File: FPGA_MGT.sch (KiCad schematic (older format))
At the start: 51 parts, among them J2 HIROSE_U.FL-R-SMT-1(10), J5 HIROSE_U.FL-R-SMT-1(10), U1 XC7A100T-2FGG484C

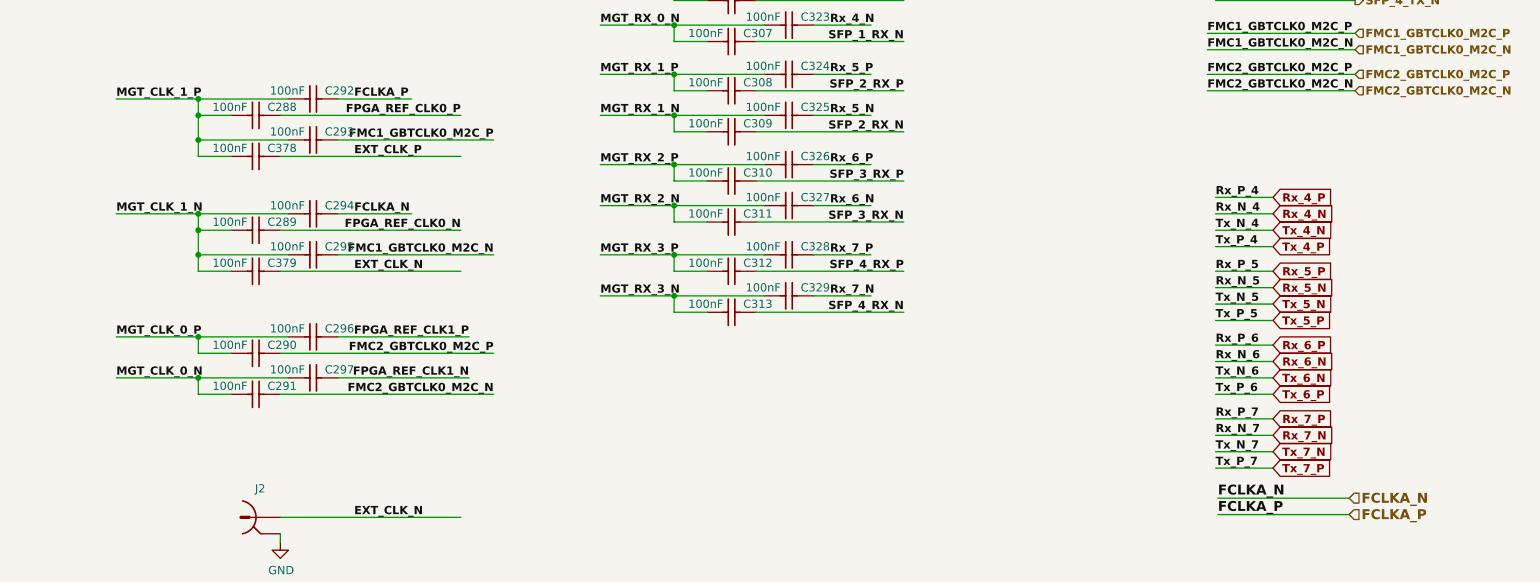
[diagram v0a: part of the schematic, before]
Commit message: added SI570, U39 3V3 -> 3V3P
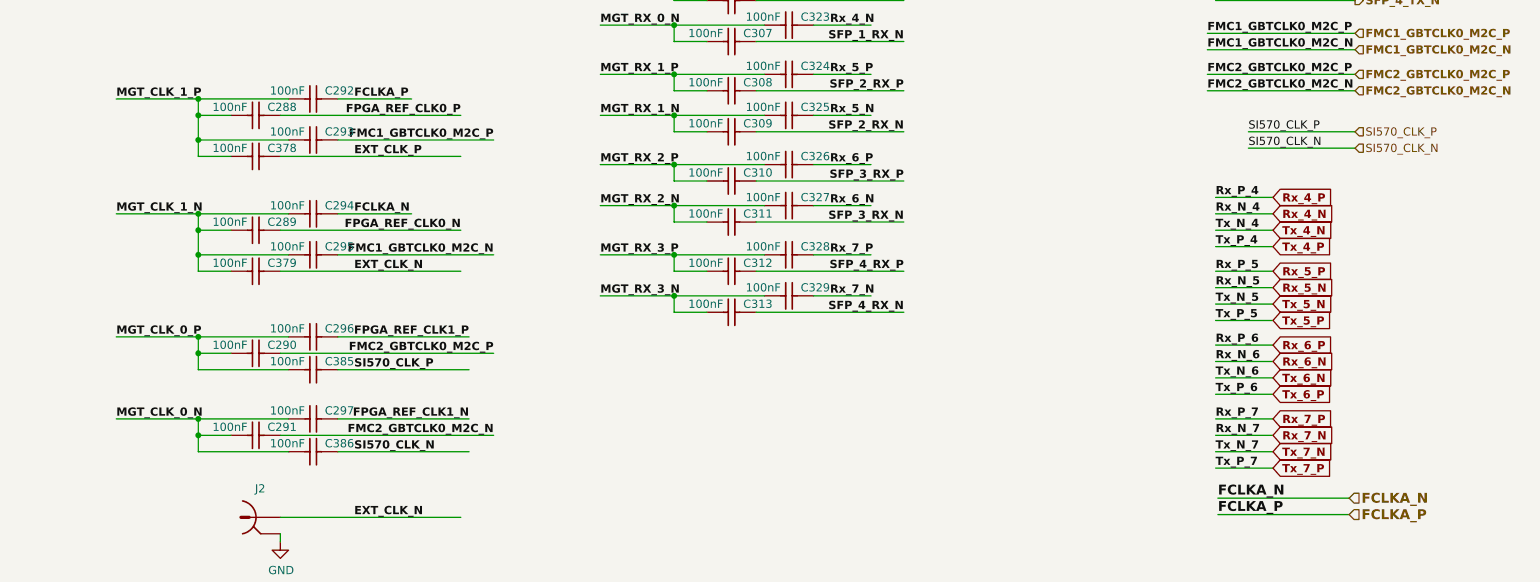
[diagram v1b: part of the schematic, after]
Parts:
- added C385, C386: CC0201_100NF_6.3V_10%_X5R, Marble:CAPC0603X33N, symbol Capacitors_SMD:CC0201_100NF_6.3V_10%_X5R
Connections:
- net labels added: SI570_CLK_N, SI570_CLK_P
- wire segments 204 -> 212
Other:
- moved on the sheet: C291, C297

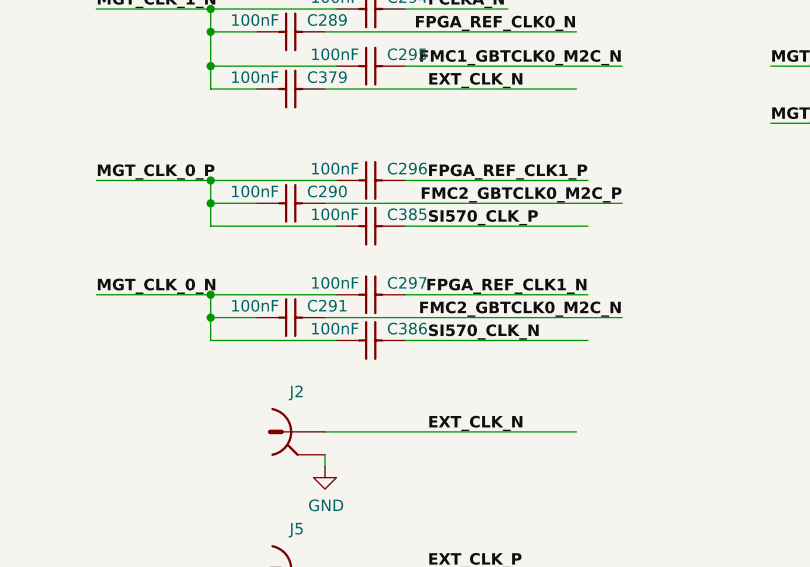
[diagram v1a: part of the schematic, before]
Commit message: More work on Si570 circuit
Attach SI570_{SCL,SDA} to I2C_APP
Make a part number for Y6 visible on schematic
Mark Y6 Si570 as dnf
Mark C385 C386 as dnf
Layout passes DRC
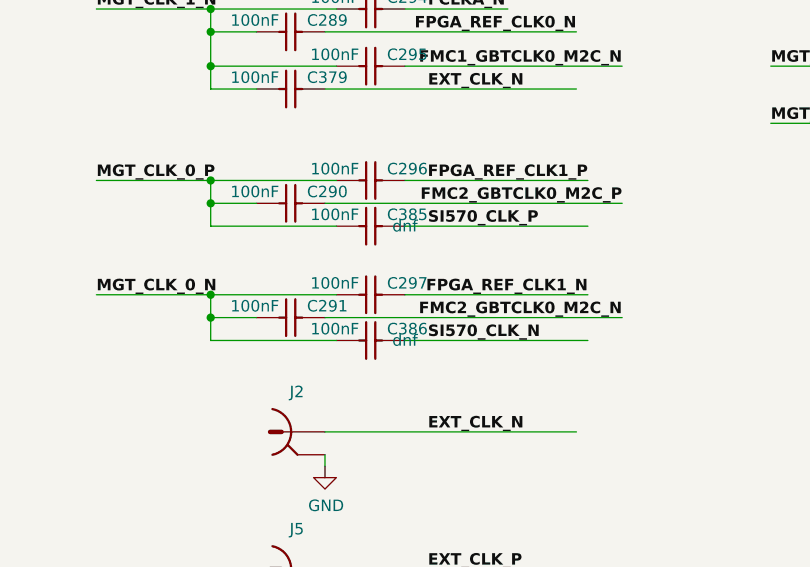
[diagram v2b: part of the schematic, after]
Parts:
- C385, C386: config (none) -> dnf
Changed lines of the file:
@@
 F 37 "Capacitors SMD" H 3500 1870 60  0001 L CNN "Library Name"
 F 38 "This work is licensed under the Creative Commons CC-BY-SA 4.0 License. To the extent that circuit schematics that use Licensed Material can be considered to be ‘Adapted Material’, then the copyright holder waives article 3.b of the license with respect to these schematics." H 3500 1780 60  0001 L CNN "License"
+F 39 "dnf" H 3500 5550 50  0000 C CNN "config"
 	1    3500 5550
 	-1   0    0    1
@@
 F 37 "Capacitors SMD" H 3500 2370 60  0001 L CNN "Library Name"
 F 38 "This work is licensed under the Creative Commons CC-BY-SA 4.0 License. To the extent that circuit schematics that use Licensed Material can be considered to be ‘Adapted Material’, then the copyright holder waives article 3.b of the license with respect to these schematics." H 3500 2280 60  0001 L CNN "License"
+F 39 "dnf" H 3500 6050 50  0000 C CNN "config"
 	1    3500 6050
 	-1   0    0    1

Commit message: schematic: clean up FPGA_MGT sheet
  * align labels
  * make config field visible
  * add a comment what the new annotation means
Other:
- note added: "-standalone"
- note added: "config fields / PCB variants"
- note added: "dnf"
- note added: "dnf when assembling Marble without AMC"
- note added: "do not fit the capacitor"
- note added: "fit the capacitor in any case"
- note added: "no annotation"
- moved on the sheet: C288, C289, C290, C291, C292, C293, C294, C295, C296, C297, C378, C379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

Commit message: SCH: add +standalone to 18 capacitors & more notes
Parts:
- C298, C299, C300, C301, C302, C303, C304, C305, C306, C307, C308, C309, C310, C311, C312, C313, C378, C379: config (none) -> +standalone
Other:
- note added: "+standalone"
- note added: "4 x SFP modules"
- note added: "8 x gigabit lanes to"
- note added: "AMC port"
- note added: "CDCM61004"
- note added: "CDCM61004 (U20)"
- note added: "U.FL connector (J2, J5)"
- note added: "default"
- note added: "dnf when assembling standalone variant"
- note added: "fit only for standalone variant"
- note added: "gigabit clock 0 from"
- note added: "gigabit clock 1 from"
- note added: "standalone"
- note removed: "dnf when assembling Marble without AMC"

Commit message: Start filling in more Manufacturer fields
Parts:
- U1: Manufacturer (none) -> Xilinx
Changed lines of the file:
@@
 F 3 "" H 2100 2150 50  0000 C CNN
 F 4 "XC7A100T-2FGG484C" H 2100 2150 50  0001 C CNN "Manufacturer Part Number"
+F 5 "Xilinx" H 2100 2150 50  0001 C CNN "Manufacturer"
 	4    2100 2150
 	-1   0    0    -1
